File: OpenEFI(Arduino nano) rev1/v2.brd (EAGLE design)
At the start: 102.7 x 102.5 mm, 85 parts, among them IC1 4050N, IC10 LM358D, IC6 74HC164D, IC7 4051D, IC8 24AA08SN, IC9 LM358D, P1 39-30-06?, Q1 MJD122, Q10 MJD122, Q11 MJD122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

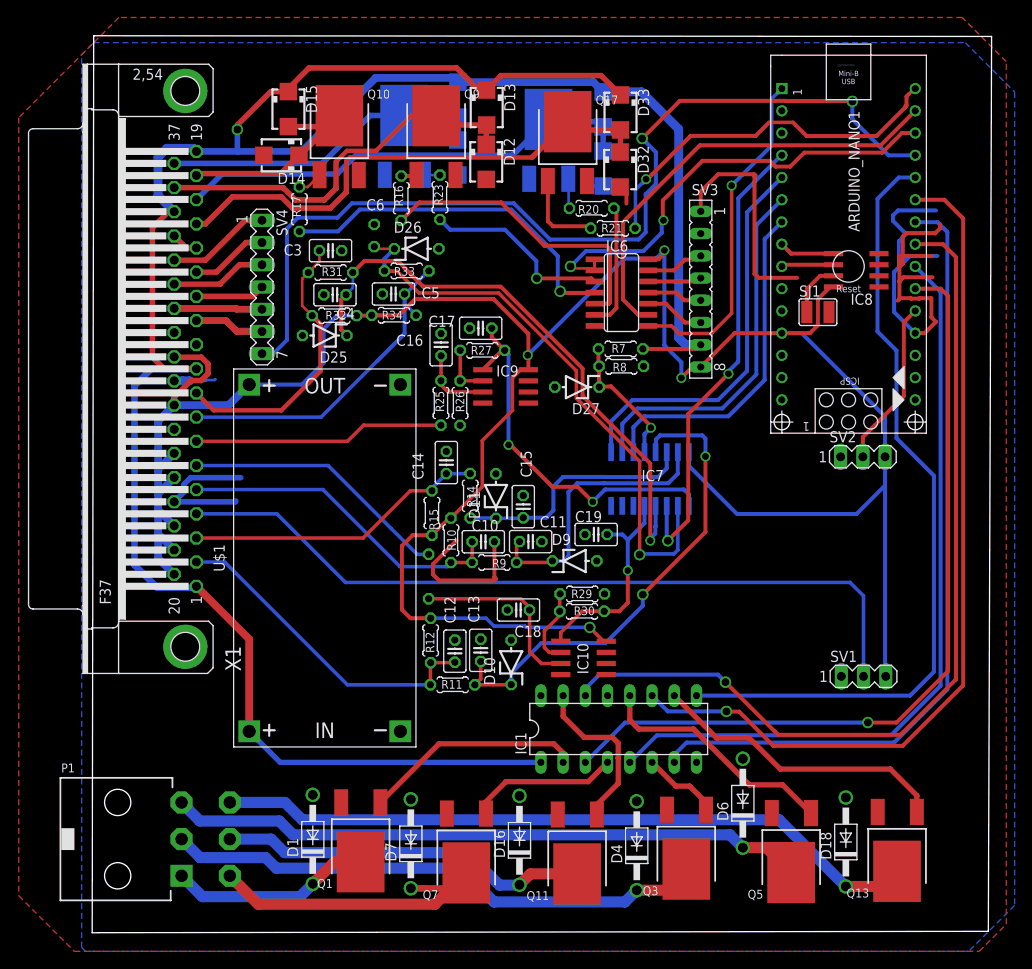
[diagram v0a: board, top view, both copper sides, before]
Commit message: Creacion de V2 del PCB para SMT32F
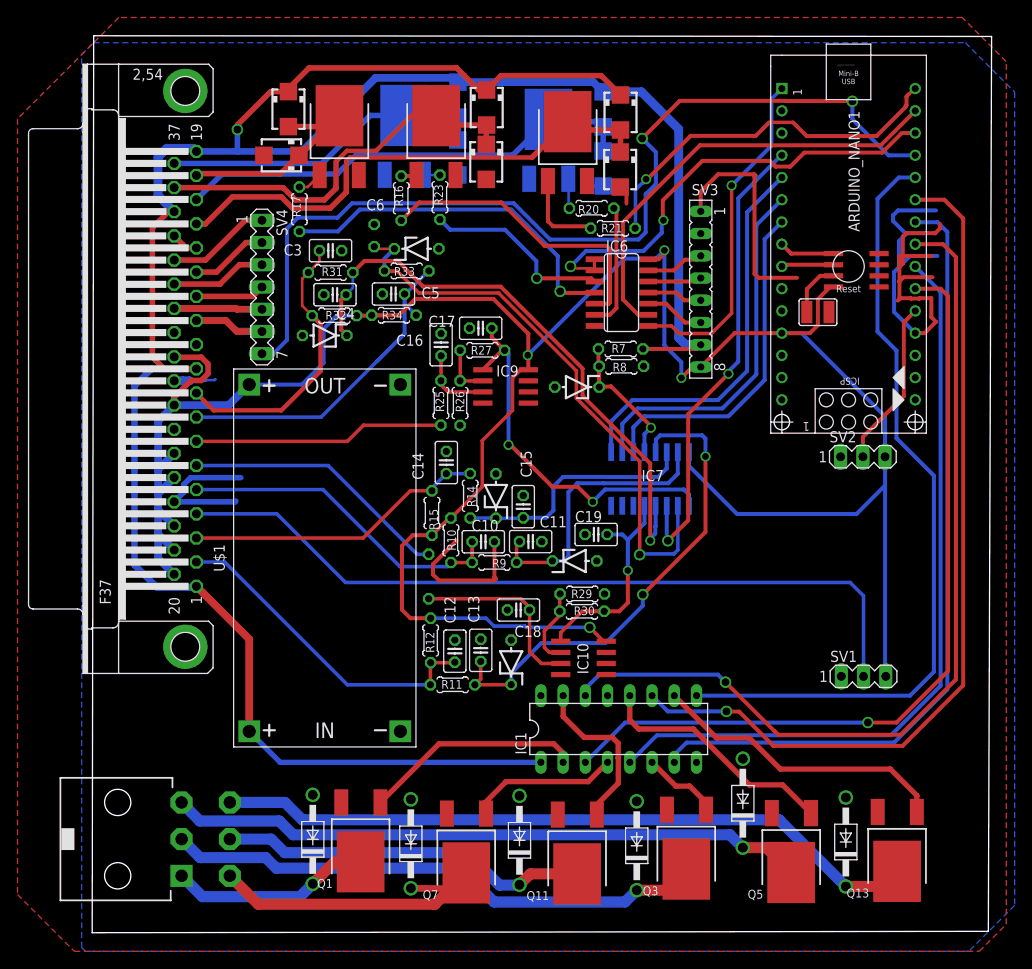
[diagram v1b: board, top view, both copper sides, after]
